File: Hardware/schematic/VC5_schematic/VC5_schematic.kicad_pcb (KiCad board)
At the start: 2 copper layers, 213.7 x 60 mm, 33 parts, among them J2 Debug_output, Q1 BC337, U1 Pico, U2 1.3in SH1106 OLED, U3 1.3in SH1106 OLED, U4 1.3in SH1106 OLED, U5 1.3in SH1106 OLED, U6 1.3in SH1106 OLED, U7 MCP23017

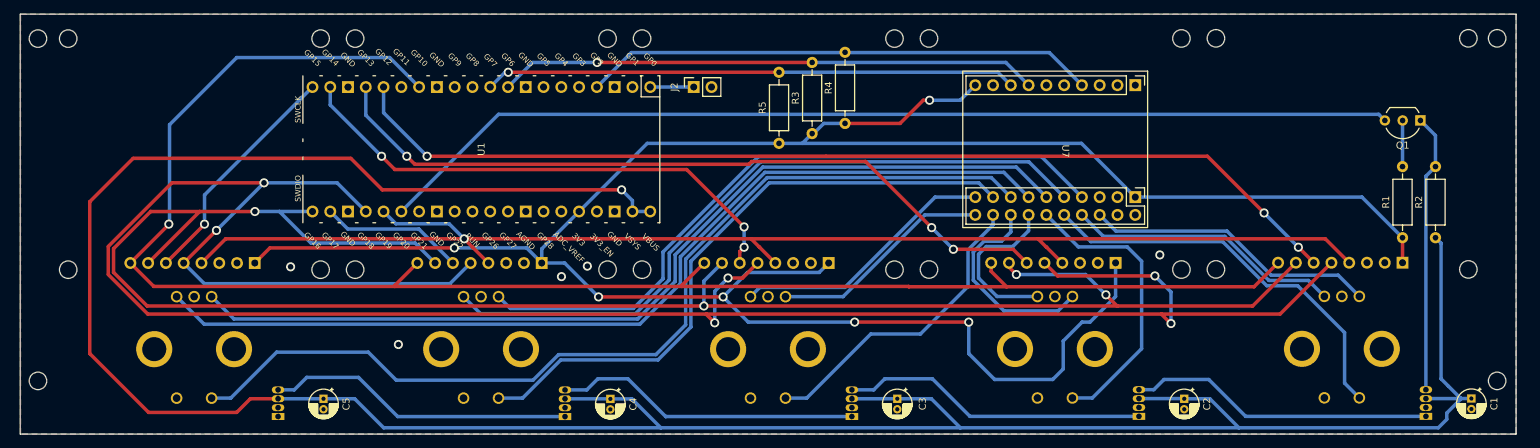
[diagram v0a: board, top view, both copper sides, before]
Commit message: reworked the PCB layout
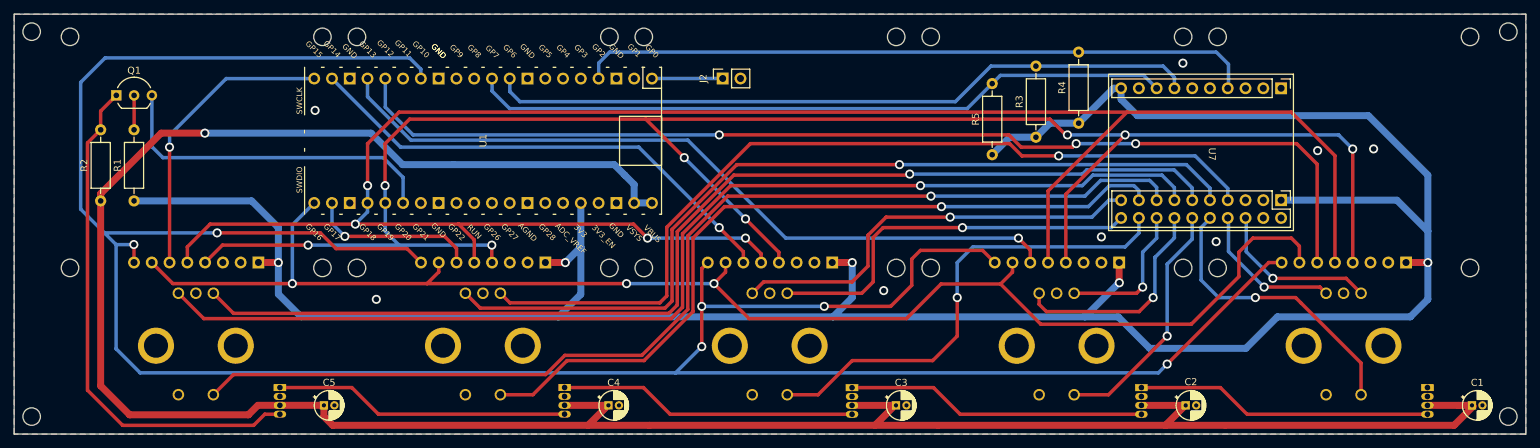
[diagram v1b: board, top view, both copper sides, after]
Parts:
- moved R2 190.8 mm to (60.0, 86.6)
- moved Q1 186.4 mm to (62.2, 71.5), turned to 0 degrees
- moved R1 181.3 mm to (64.7, 86.6)
- moved R4 33.4 mm to (199.7, 75.5)
- moved R3 32.0 mm to (193.6, 77.5)
- moved R5 30.5 mm to (187.3, 80.0)
- moved U7 20.8 mm to (217.2, 78.9)
- moved VR4 8.07 mm to (114.6, 107.2)
- moved VR5 8.07 mm to (73.6, 107.2)
- moved VR3 8.06 mm to (155.6, 107.2)
- moved VR2 8.04 mm to (196.6, 107.2)
- moved VR1 8.03 mm to (237.6, 107.2)
- moved ? 5.35 mm to (261.1, 117.4)
- moved ? 5.18 mm to (50.1, 117.4)
- moved J2 4.31 mm to (148.8, 69.1)
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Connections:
- D1 pad 1: Net-(D1-DO) -> unconnected-(D1-DO-Pad1)
- D2 pad 1: Net-(D2-DO) -> Net-(D1-DI)
- D2 pad 4: Net-(D1-DO) -> Net-(D2-DI)
- D3 pad 1: Net-(D3-DO) -> Net-(D2-DI)
- D3 pad 4: Net-(D2-DO) -> Net-(D3-DI)
- D4 pad 1: Net-(D4-DO) -> Net-(D3-DI)
- D4 pad 4: Net-(D3-DO) -> Net-(D4-DI)
- D5 pad 1: unconnected-(D5-DO-Pad1) -> Net-(D4-DI)
- D5 pad 4: Net-(D4-DO) -> Net-(D5-DI)
- Q1 pad 1: Net-(D1-DI) -> Net-(D5-DI)
- R2 pad 2: Net-(D1-DI) -> Net-(D5-DI)
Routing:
- net DISP_RESET: track 244.0 -> 384.6 mm, vias 1 -> 6
- net LED: track 146.7 -> 48.7 mm
- net Net-(D5-DI): track 0.00 -> 74.1 mm
- net DIN: track 194.7 -> 267.6 mm, vias 1 -> 8
- net D/C: track 268.8 -> 205.7 mm, vias 4 -> 3
- net Net-(D4-DO): track 44.1 -> 0.00 mm
- net Net-(D2-DO): track 43.9 -> 0.00 mm
- net Net-(D3-DO): track 43.9 -> 0.00 mm
- net Net-(D1-DO): track 43.8 -> 0.00 mm
- net Net-(D2-DI): track 0.00 -> 42.9 mm
- net Net-(D3-DI): track 0.00 -> 42.7 mm
- net Net-(D4-DI): track 0.00 -> 42.2 mm
- net +5V: track 392.5 -> 354.7 mm
- net CLK: track 327.0 -> 291.3 mm, vias 6 -> 4
- net +3.3V: track 332.1 -> 366.0 mm, vias 6 -> 5
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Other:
- board size 213.7 x 60 mm -> 216 x 60 mm

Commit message: small adjustments to the positions of  the components
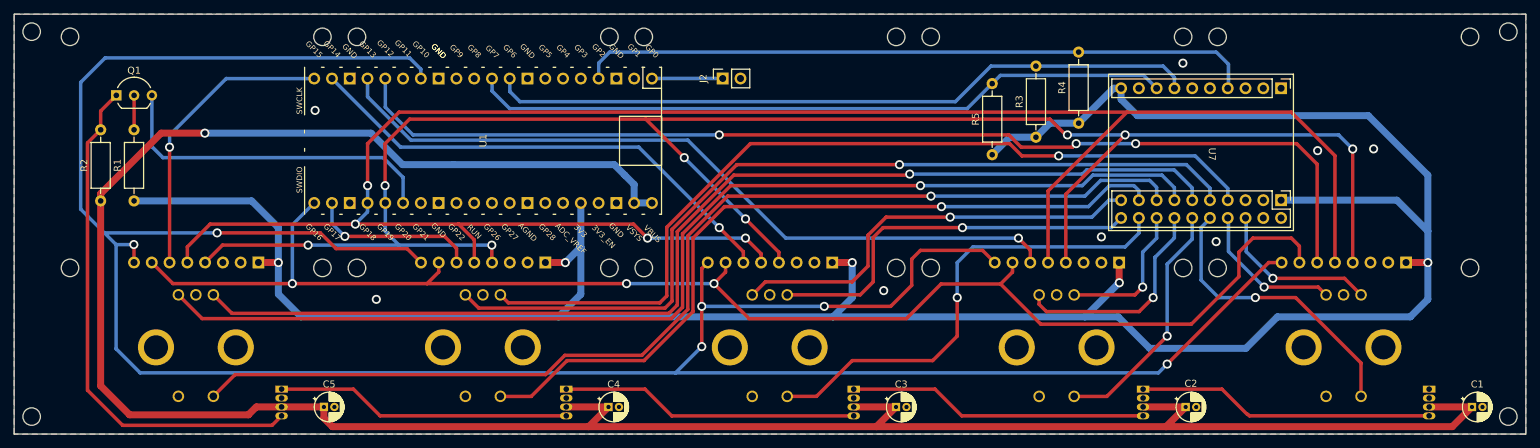
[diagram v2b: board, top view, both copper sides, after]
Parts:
- moved D4 0.34 mm to (126.5, 113.5)
- moved D5 0.33 mm to (85.8, 113.5)
- moved D1 0.33 mm to (249.8, 113.5)
- moved D2 0.33 mm to (208.9, 113.5)
- moved D3 0.33 mm to (167.6, 113.5)
- moved C1 0.23 mm to (255.9, 116.0)
- moved C2 0.23 mm to (215.0, 116.0)
- moved C3 0.23 mm to (173.6, 116.0)
- moved C4 0.23 mm to (132.5, 116.0)
- moved C5 0.23 mm to (91.9, 116.0)
- moved VR1 0.23 mm to (237.6, 107.4)
- moved VR2 0.23 mm to (196.6, 107.4)
- moved VR3 0.23 mm to (155.6, 107.4)
- moved VR4 0.23 mm to (114.6, 107.4)
- moved VR5 0.23 mm to (73.6, 107.4)
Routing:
- net +5V: track 354.7 -> 353.1 mm
- net Net-(D4-DI): track 42.2 -> 42.7 mm
